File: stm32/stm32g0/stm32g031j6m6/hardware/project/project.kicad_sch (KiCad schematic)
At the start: 4 parts

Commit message: working on minimal setup
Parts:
- added D? (x2): LED, symbol Device:LED
- added R? (x2): R, symbol Device:R
- added U?: JTAG_10, symbol lib:JTAG_10
- C?: value (none) -> 10uf
- C?: value (none) -> 22uf
- U?: value (none) -> STM32G031J6M6
- U?: value (none) -> AZ1117-3.3
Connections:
- net GND: now also R?.1, R?.1, U?.3, U?.5, U?.9
- net NRST: now reaches U?.4 (PA0/PA1/PA2/PF2-NRST)
- net NRST: now also U?.10
- net LED_2: now reaches U?.6 (PA12[PA10])
- net LED_2: now also D?.2 (A)
- net LED_1: now reaches U?.7 (PA13)
- net LED_1: now also D?.2 (A)
- new net: D?.1 (K), R?.2 (x2)
- new net SWCLK: U?.4
- new net SWDIO: U?.2
- new net VCC: U?.1

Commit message: Assigning footprints
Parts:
- D1, D2: renamed from D?; footprint (none) -> LED_SMD:LED_0805_2012Metric
- R1, R2: renamed from R?; footprint (none) -> Resistor_SMD:R_0805_2012Metric
- gave numbers to parts that had none: 5

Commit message: added footprint for reg
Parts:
- U1: footprint (none) -> Package_TO_SOT_SMD:TO-252-3_TabPin2
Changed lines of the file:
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@@
     (property "Reference" "U1" (id 0) (at 39.37 17.78 0))
     (property "Value" "AZ1117-3.3" (id 1) (at 39.37 20.32 0))
-    (property "Footprint" "" (id 2) (at 39.37 19.05 0)
+    (property "Footprint" "Package_TO_SOT_SMD:TO-252-3_TabPin2" (id 2) (at 39.37 19.05 0)
       (effects (font (size 1.27 1.27) italic) hide)
     )
@@
     )
     (path "/ee930e55-2ff2-46ef-8929-34a921d8e7be"
-      (reference "U1") (unit 1) (value "AZ1117-3.3") (footprint "")
+      (reference "U1") (unit 1) (value "AZ1117-3.3") (footprint "Package_TO_SOT_SMD:TO-252-3_TabPin2")
     )
     (path "/f2302342-dc6c-4c64-ac72-559cbd681654"

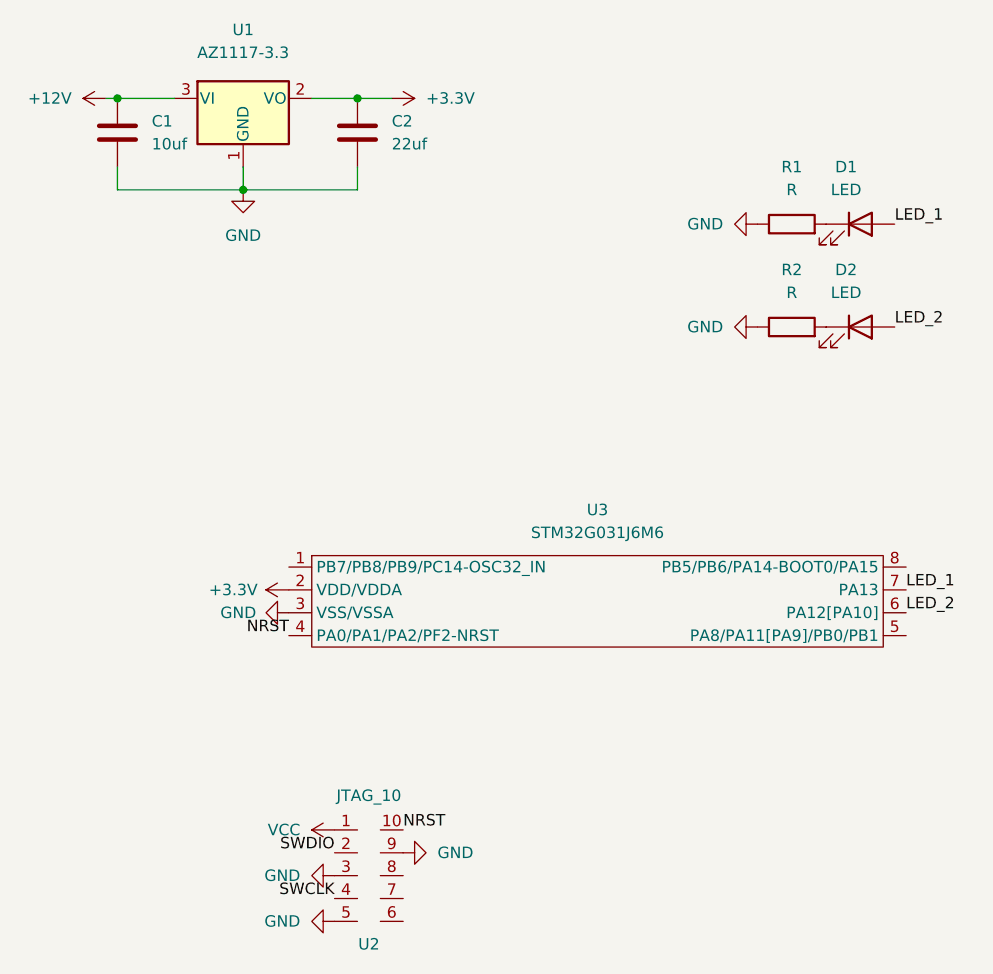
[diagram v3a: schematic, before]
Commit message: Moved to 3.3v instead of VCC
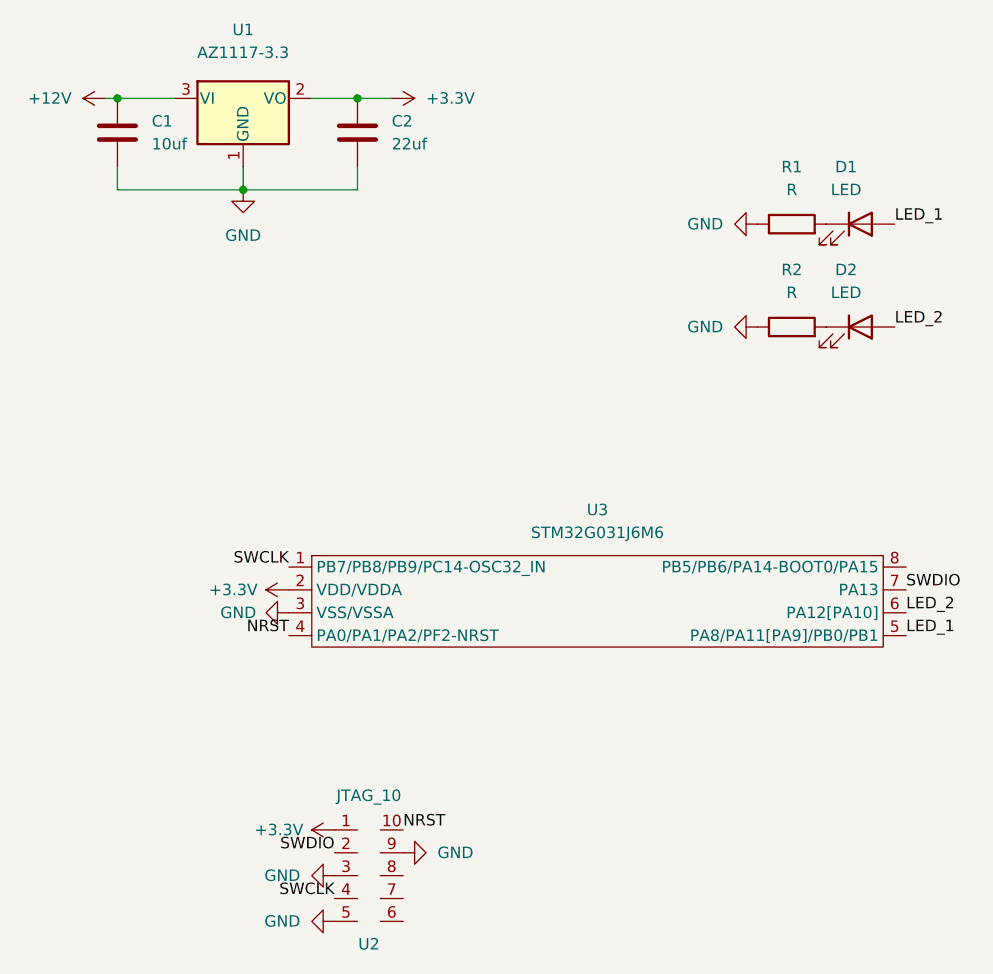
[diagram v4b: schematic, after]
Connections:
- net VCC is gone; now on net +3V3: U2.1
- net LED_1: now also U3.5 (PA8/PA11[PA9]/PB0/PB1); no longer U3.7 (PA13)
- net SWCLK: now also U3.1 (PB7/PB8/PB9/PC14-OSC32_IN)
- net SWDIO: now also U3.7 (PA13)
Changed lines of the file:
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@@
     (effects (font (size 1.27 1.27)) (justify left bottom))
   )
-  (label "LED_1" (at 113.03 80.01 0)
+  (label "LED_1" (at 113.03 85.09 0)
     (effects (font (size 1.27 1.27)) (justify left bottom))
   )
@@
     (effects (font (size 1.27 1.27)) (justify right bottom))
   )
+  (label "SWCLK" (at 44.45 77.47 180)
+    (effects (font (size 1.27 1.27)) (justify right bottom))
+  )
   (label "SWCLK" (at 49.53 114.3 180)
     (effects (font (size 1.27 1.27)) (justify right bottom))
+  )
+  (label "SWDIO" (at 113.03 80.01 0)
+    (effects (font (size 1.27 1.27)) (justify left bottom))
   )
   (label "LED_2" (at 111.76 50.8 0)
@@
     (pin "8")
   )
+  (symbol (lib_id "power:+3.3V") (at 49.53 106.68 90) (unit 1)
+    (in_bom yes) (on_board yes)
+    (property "Reference" "#PWR0109" (id 0) (at 53.34 106.68 0)
+      (effects (font (size 1.27 1.27)) hide)
+    )
+    (property "Value" "+3.3V" (id 1) (at 40.64 106.68 90)
+      (effects (font (size 1.27 1.27)) (justify right))
+    )
+    (property "Footprint" "" (id 2) (at 49.53 106.68 0)
+      (effects (font (size 1.27 1.27)) hide)
+    )
+    (property "Datasheet" "" (id 3) (at 49.53 106.68 0)
+      (effects (font (size 1.27 1.27)) hide)
+    )
+    (pin "1")
+  )
   (symbol (lib_id "power:GND") (at 57.15 109.22 90) (unit 1)
     (in_bom yes) (on_board yes) (fields_autoplaced)
@@
     )
     (property "Datasheet" "" (id 3) (at 55.88 25.4 0)
-      (effects (font (size 1.27 1.27)) hide)
-    )
-    (pin "1")
-  )
-  (symbol (lib_id "power:VCC") (at 49.53 106.68 90) (unit 1)
-    (in_bom yes) (on_board yes) (fields_autoplaced)
-    (property "Reference" "#PWR0109" (id 0) (at 53.34 106.68 0)
-      (effects (font (size 1.27 1.27)) hide)
-    )
-    (property "Value" "VCC" (id 1) (at 45.72 106.6799 90)
-      (effects (font (size 1.27 1.27)) (justify left))
-    )
-    (property "Footprint" "" (id 2) (at 49.53 106.68 0)
-      (effects (font (size 1.27 1.27)) hide)
-    )
-    (property "Datasheet" "" (id 3) (at 49.53 106.68 0)
       (effects (font (size 1.27 1.27)) hide)
     )
@@
       (reference "#PWR0108") (unit 1) (value "GND") (footprint "")
     )
-    (path "/8c72ba3b-cf5b-40d1-bdd3-16a6219cd078"
-      (reference "#PWR0109") (unit 1) (value "VCC") (footprint "")
+    (path "/1e52e85c-945d-4001-aabc-ccb2f3a0f502"
+      (reference "#PWR0109") (unit 1) (value "+3.3V") (footprint "")
     )
     (path "/61044edb-9068-4b6c-8504-1a3ed54d269b"
